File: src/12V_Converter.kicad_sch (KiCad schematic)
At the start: 37 parts, among them M4 CSD19534Q5A, M5 NVMFS6H836NLT1G, U2 LM5190RGYR_(20V-50V)

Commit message: Updated symbols
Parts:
- removed M5: NVMFS6H836NLT1G, PowerPCB_Footprints:NVMFS6H836NLT1G, symbol Schlib1:NVMFS6H836NLT1G
- removed Net Tie1: 0, powerDristributionBoard-import-fps:RESC0603X28X15NL05T05, symbol Altium Content Vault:RES
- added M3: NVMFS6H836NLT1G, PowerPCB_Footprints:NVMFS6H836NLT1G, symbol PowerPCB_Symbols:NVMFS6H836NLT1G
- added NT1: NetTie_2, symbol Device:NetTie_2
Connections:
- net GND: now also M3.1 (S), M3.2 (S), M3.3 (S), NT1.1
- net GNDA: now also NT1.2
- net at C18.2, L1.1, M4.1 (S)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: now also M3.5 (D)
- net at U2.9 (LO): now also M3.4 (G)

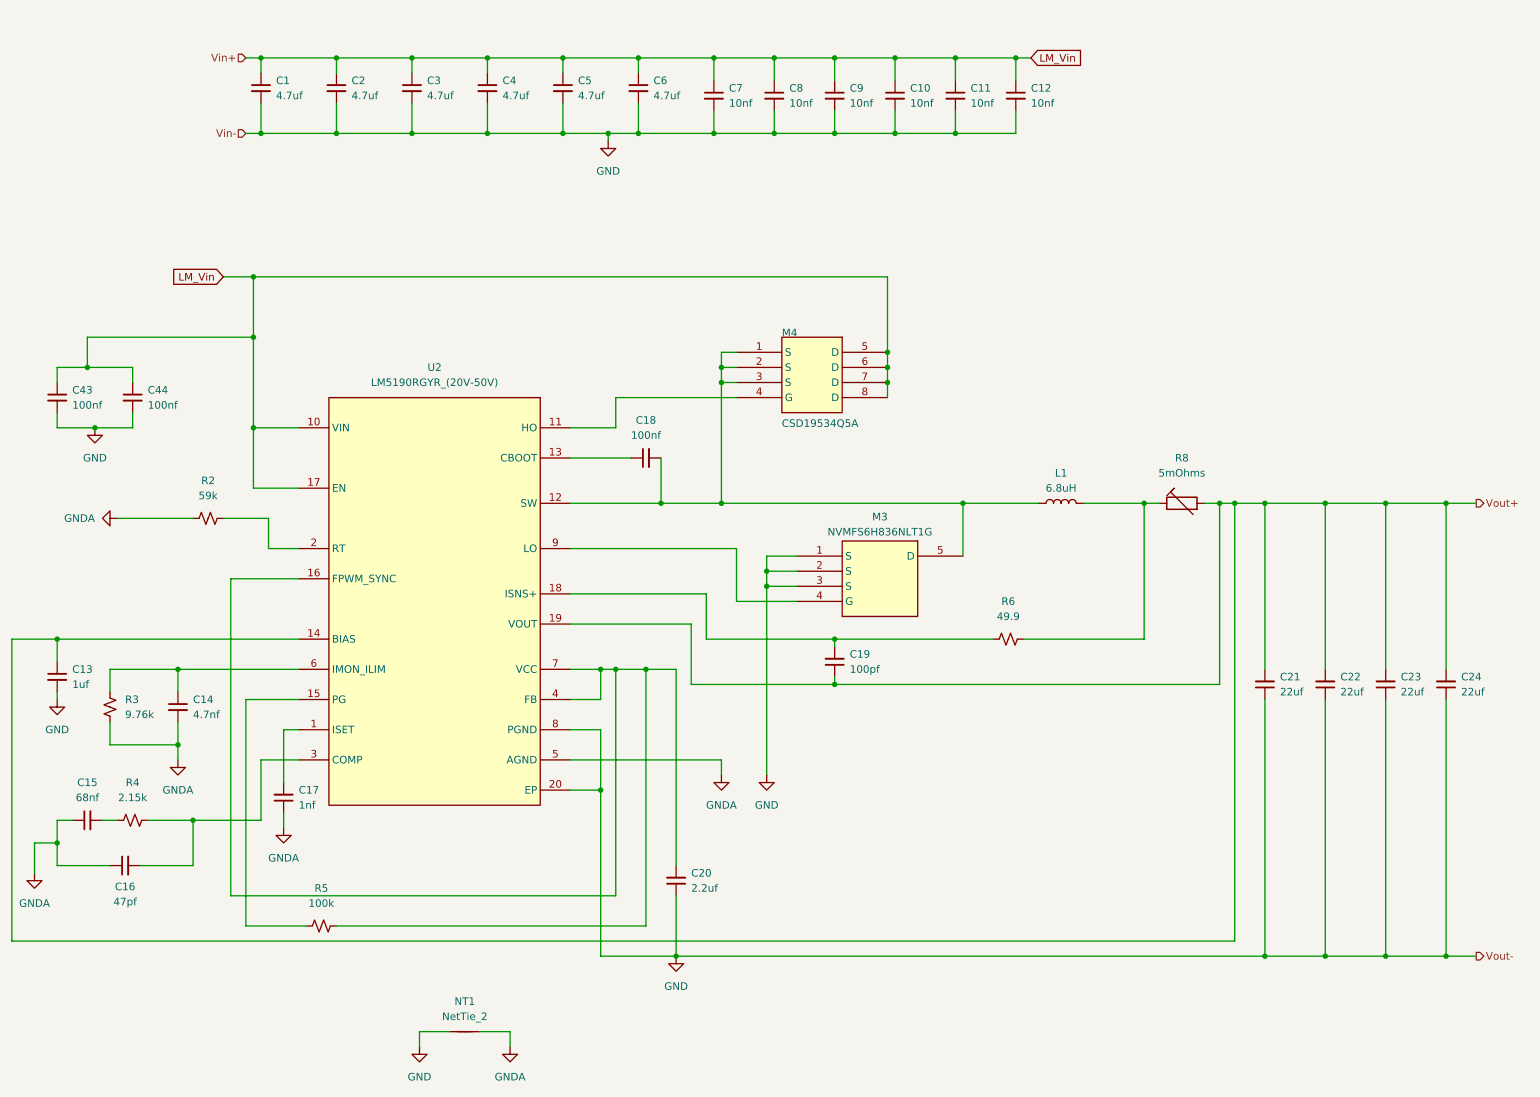
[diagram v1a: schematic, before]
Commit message: Added more components
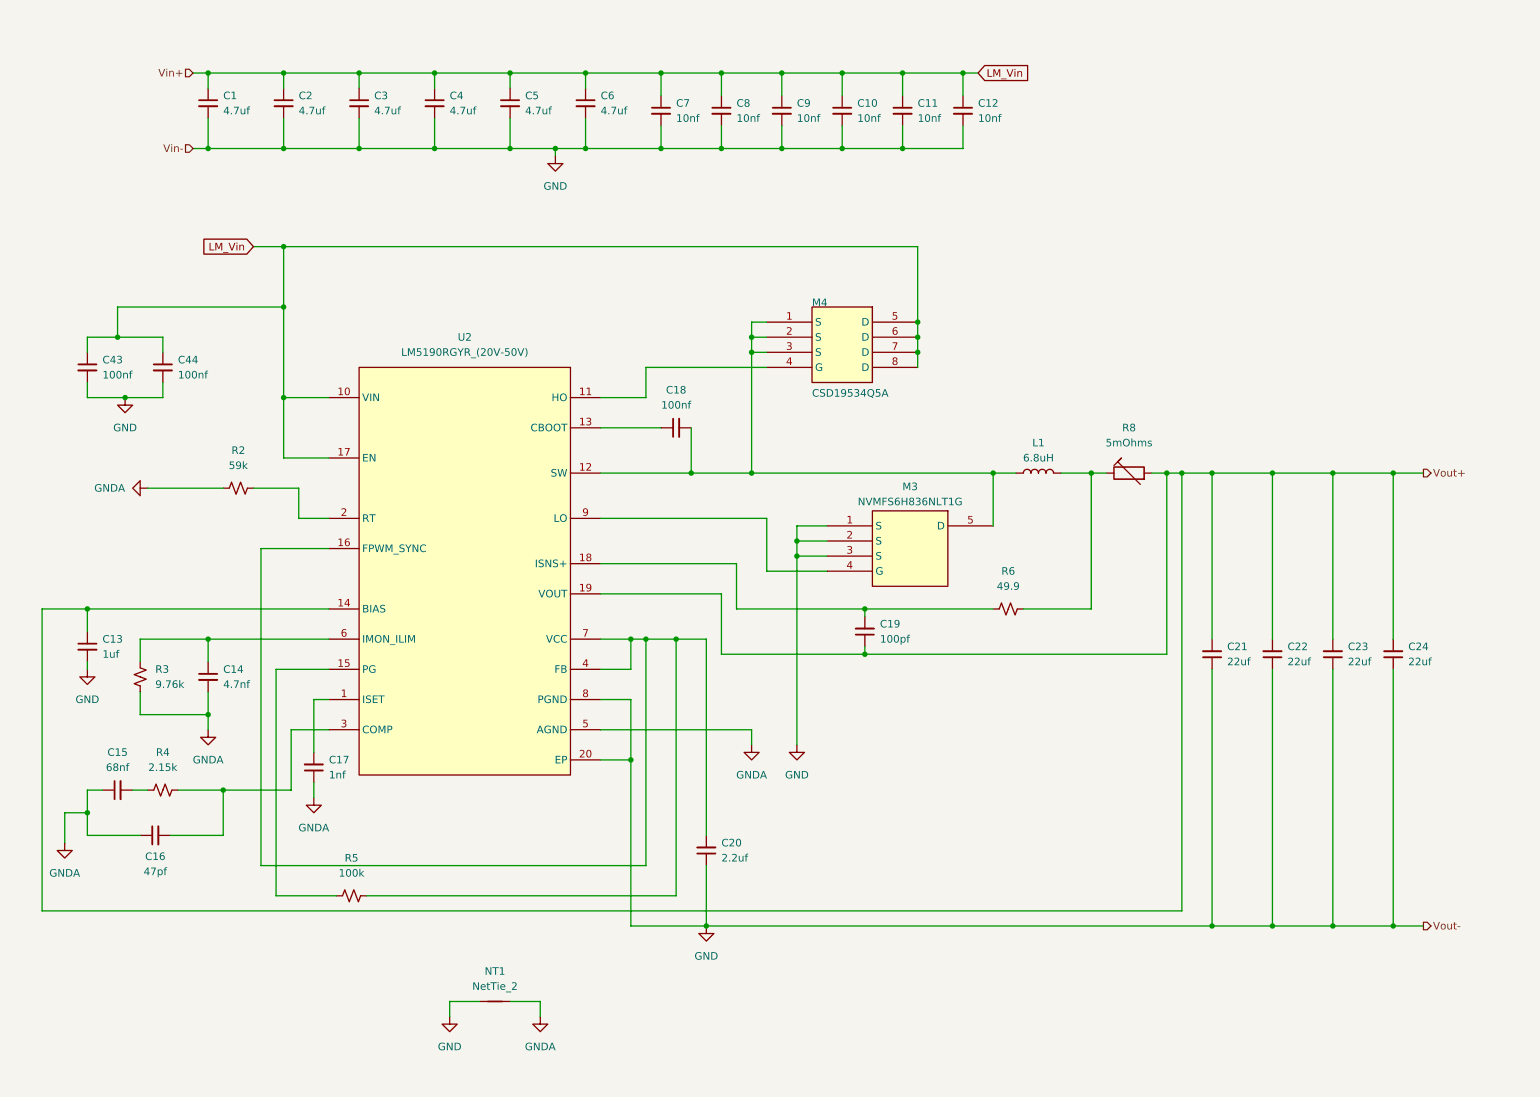
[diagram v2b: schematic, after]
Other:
- moved on the sheet: C1, C10, C11, C12, C13, C14, C15, C16, C17, C18, C19, C2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

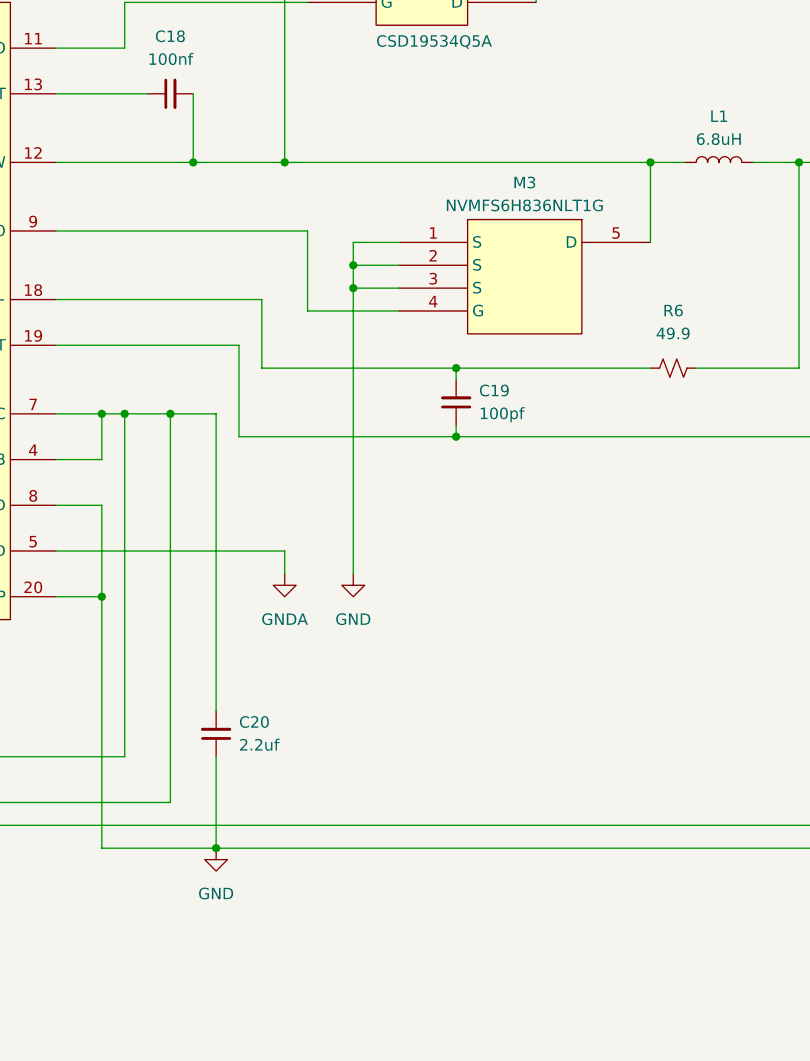
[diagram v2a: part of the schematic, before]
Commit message: Redesigned 5V regulator and edited libraries
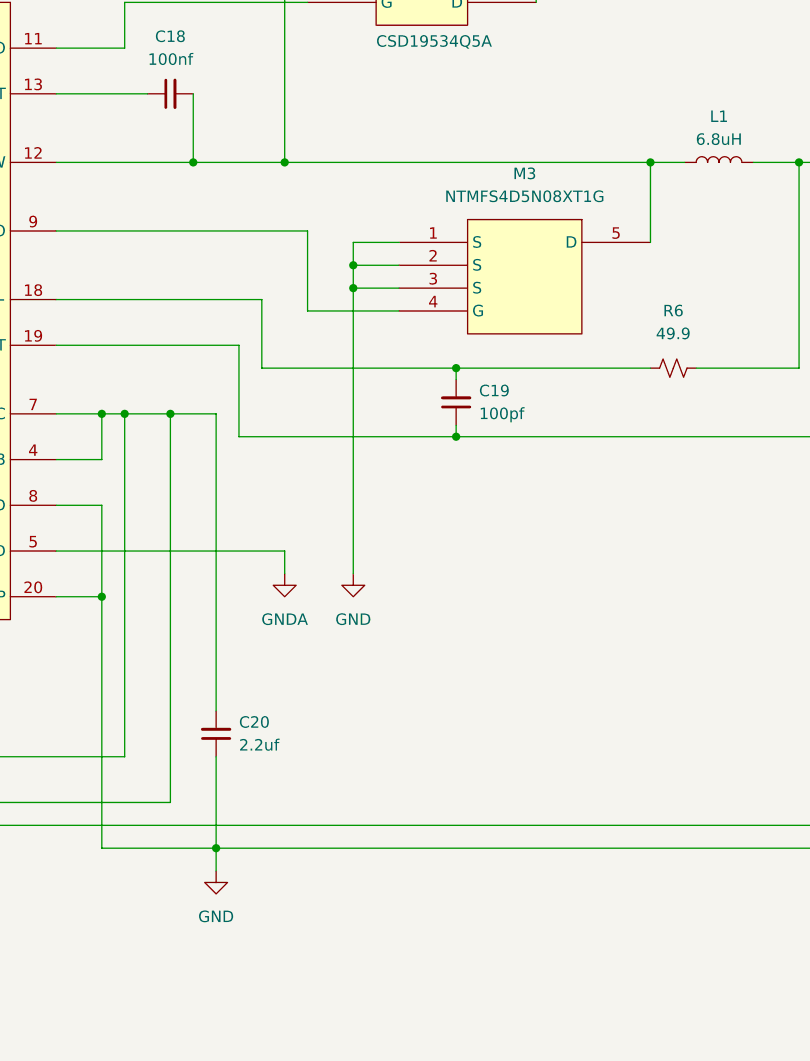
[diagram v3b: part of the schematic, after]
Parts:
- removed M3: NVMFS6H836NLT1G, PowerPCB_Footprints:NVMFS6H836NLT1G, symbol PowerPCB_Symbols:NVMFS6H836NLT1G
- added M3: NTMFS4D5N08XT1G, PowerPCB_Footprints:NTMFS4D5N08XT1G, symbol PowerPCB_Symbols:NTMFS4D5N08XT1G
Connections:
- net GND: now also M3.1 (S), M3.2 (S), M3.3 (S)
- net at C18.2, L1.1, M4.1 (S)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: now also M3.5 (D)
- net at U2.9 (LO): now also M3.4 (G)
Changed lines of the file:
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@@
 	(wire
 		(pts
+			(xy 132.08 170.18) (xy 132.08 167.64)
+		)
+		(stroke
+			(width 0)
+			(type default)
+		)
+	)
+	(wire
+		(pts
 			(xy 247.65 167.64) (xy 247.65 124.46)
 		)
@@
 	)
 	(symbol
+		(lib_id "PowerPCB_Symbols:NTMFS4D5N08XT1G")
+		(at 172.72 113.03 0)
+		(unit 1)
+		(body_style 1)
+		(exclude_from_sim no)
+		(in_bom yes)
+		(on_board yes)
+		(in_pos_files yes)
+		(dnp no)
+		(fields_autoplaced yes)
+		(property "Reference" "M3"
+			(at 166.37 92.71 0)
+			(show_name no)
+			(do_not_autoplace no)
+			(effects
+				(font
+					(size 1.27 1.27)
+				)
+			)
+		)
+		(property "Value" "NTMFS4D5N08XT1G"
+			(at 166.37 95.25 0)
+			(show_name no)
+			(do_not_autoplace no)
+			(effects
+				(font
+					(size 1.27 1.27)
+				)
+			)
+		)
+		(property "Footprint" "PowerPCB_Footprints:NTMFS4D5N08XT1G"
+			(at 172.72 113.03 0)
+			(hide yes)
+			(show_name no)
+			(do_not_autoplace no)
+			(effects
+				(font
+					(size 1.27 1.27)
+				)
+			)
+		)
+		(property "Datasheet" ""
+			(at 172.72 113.03 0)
+			(hide yes)
+			(show_name no)
+			(do_not_autoplace no)
+			(effects
+				(font
+					(size 1.27 1.27)
+				)
+			)
+		)
+		(property "Description" ""
+			(at 172.72 113.03 0)
+			(hide yes)
+			(show_name no)
+			(do_not_autoplace no)
+			(effects
+				(font
+					(size 1.27 1.27)
+				)
+			)
+		)
+		(pin "1"
+		)
+		(pin "4"
+		)
+		(pin "3"
+		)
+		(pin "2"
+		)
+		(pin "5"
+		)
+		(instances
+			(project "powerDristributionBoard"
+				(path "/501e9f3f-9bfa-47dd-b56d-5fd6974f0d03/8cad4ca2-ba0b-4eb3-ba1b-4233b97b1d3e"
+					(reference "M3")
+					(unit 1)
+				)
+			)
+		)
+	)
+	(symbol
 		(lib_id "Device:C_Small")
 		(at 48.26 29.21 0)
@@
 	)
 	(symbol
-		(lib_id "PowerPCB_Symbols:NVMFS6H836NLT1G")
-		(at 172.72 113.03 0)
-		(unit 1)
-		(body_style 1)
-		(exclude_from_sim no)
-		(in_bom yes)
-		(on_board yes)
-		(in_pos_files yes)
-		(dnp no)
-		(property "Reference" "M3"
-			(at 166.37 93.726 0)
-			(show_name no)
-			(do_not_autoplace no)
-			(effects
-				(font
-					(size 1.27 1.27)
-				)
-			)
-		)
-		(property "Value" "NVMFS6H836NLT1G"
-			(at 166.37 96.266 0)
-			(show_name no)
-			(do_not_autoplace no)
-			(effects
-				(font
-					(size 1.27 1.27)
-				)
-			)
-		)
-		(property "Footprint" "PowerPCB_Footprints:NVMFS6H836NLT1G"
-			(at 172.72 113.03 0)
-			(hide yes)
-			(show_name no)
-			(do_not_autoplace no)
-			(effects
-				(font
-					(size 1.27 1.27)
-				)
-			)
-		)
-		(property "Datasheet" ""
-			(at 172.72 113.03 0)
-			(hide yes)
-			(show_name no)
-			(do_not_autoplace no)
-			(effects
-				(font
-					(size 1.27 1.27)
-				)
-			)
-		)
-		(property "Description" ""
-			(at 172.72 113.03 0)
-			(hide yes)
-			(show_name no)
-			(do_not_autoplace no)
-			(effects
-				(font
-					(size 1.27 1.27)
-				)
-			)
-		)
-		(pin "1"
-		)
-		(pin "5"
-		)
-		(pin "3"
-		)
-		(pin "4"
-		)
-		(pin "2"
-		)
-		(instances
-			(project "powerDristributionBoard"
-				(path "/501e9f3f-9bfa-47dd-b56d-5fd6974f0d03/8cad4ca2-ba0b-4eb3-ba1b-4233b97b1d3e"
-					(reference "M3")
-					(unit 1)
-				)
-			)
-		)
-	)
-	(symbol
 		(lib_id "Device:C_Small")
 		(at 99.06 29.21 0)
@@
 	(symbol
 		(lib_id "power:GND")
-		(at 132.08 167.64 0)
+		(at 132.08 170.18 0)
 		(unit 1)
 		(body_style 1)
@@
 		(fields_autoplaced yes)
 		(property "Reference" "#PWR06"
-			(at 132.08 173.99 0)
+			(at 132.08 176.53 0)
 			(hide yes)
 			(show_name no)
@@
 		)
 		(property "Value" "GND"
-			(at 132.08 172.72 0)
+			(at 132.08 175.26 0)
 			(show_name no)
 			(do_not_autoplace no)
@@
 		)
 		(property "Footprint" ""
-			(at 132.08 167.64 0)
+			(at 132.08 170.18 0)
 			(hide yes)
 			(show_name no)
@@
 		)
 		(property "Datasheet" ""
-			(at 132.08 167.64 0)
+			(at 132.08 170.18 0)
 			(hide yes)
 			(show_name no)
@@
 		)
 		(property "Description" "Power symbol creates a global label with name \"GND\" , ground"
-			(at 132.08 167.64 0)
+			(at 132.08 170.18 0)
 			(hide yes)
 			(show_name no)

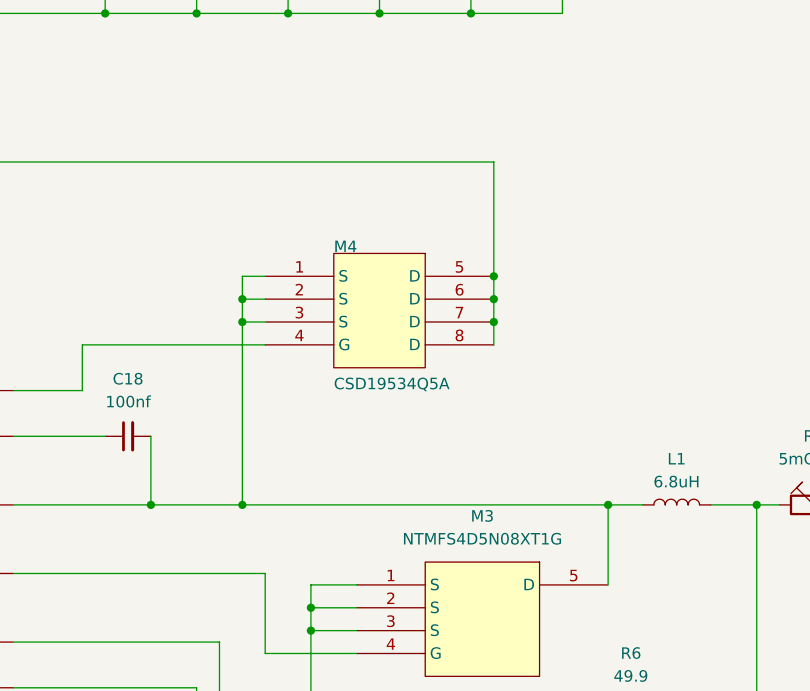
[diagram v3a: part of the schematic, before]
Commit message: Redesigned 5V regulator and added more parts
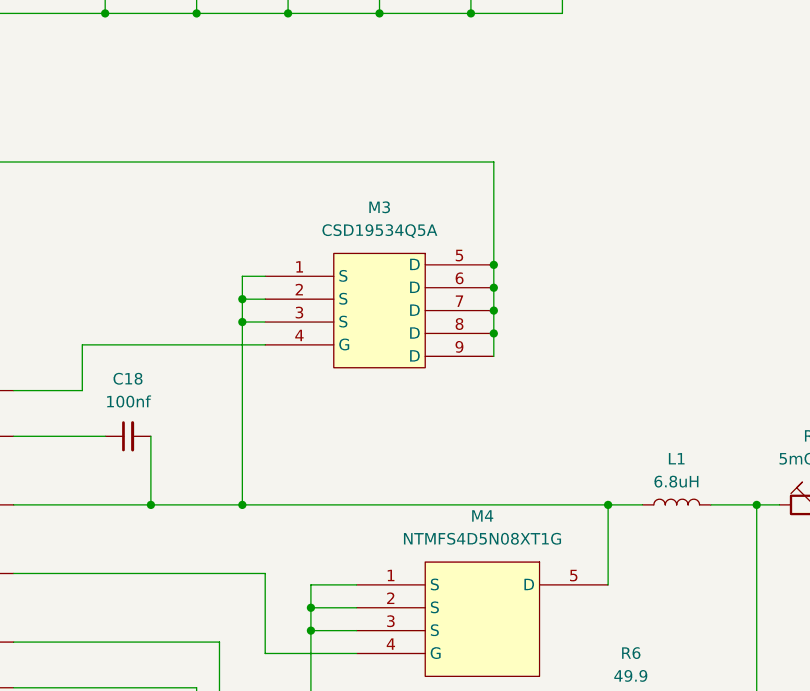
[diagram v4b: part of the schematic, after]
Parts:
- removed M4: CSD19534Q5A, PowerPCB_Footprints:CSD19534Q5A, symbol Schlib1:CSD19534Q5A
- added M3: CSD19534Q5A, PowerPCB_Footprints:CSD19534Q5A, symbol PowerPCB_Symbols:CSD19534Q5A
- renumbered M3 to M4
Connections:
- net LM_Vin: now also M3.5 (D), M3.6 (D), M3.7 (D), M3.8 (D), M3.9 (D)
- net at C18.2, L1.1, M4.5 (D)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: now also M3.1 (S), M3.2 (S), M3.3 (S)
- net at U2.11 (HO): now also M3.4 (G)

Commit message: Finalized schematic
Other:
- moved on the sheet: R3

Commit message: Edited PCB layout
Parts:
- C32: renamed from C21; now not fitted
- C33: renamed from C22; now not fitted
- C34: renamed from C23; now not fitted
- C35: renamed from C24; now not fitted
- renumbered C43 to C10, C13 to C11, C15 to C12, C44 to C13, C16 to C14, C1 to C15, C14 to C16, C2 to C17, C17 to C18, C3 to C19, C4 to C20, C5 to C21, C6 to C22, C7 to C23, C18 to C24, C20 to C25, C8 to C26, C9 to C27, C10 to C28, C19 to C29, C11 to C30, C12 to C31, R3 to R10, R4 to R11, R2 to R12, R5 to R13, R6 to R14, R8 to R15

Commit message: Edited PCB layout
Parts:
- C32, C33, C34, C35: now fitted
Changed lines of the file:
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@@
 		(on_board yes)
 		(in_pos_files yes)
-		(dnp yes)
+		(dnp no)
 		(fields_autoplaced yes)
 		(property "Reference" "C34"
@@
 		(on_board yes)
 		(in_pos_files yes)
-		(dnp yes)
+		(dnp no)
 		(fields_autoplaced yes)
 		(property "Reference" "C35"
@@
 		(on_board yes)
 		(in_pos_files yes)
-		(dnp yes)
+		(dnp no)
 		(fields_autoplaced yes)
 		(property "Reference" "C32"
@@
 		(on_board yes)
 		(in_pos_files yes)
-		(dnp yes)
+		(dnp no)
 		(fields_autoplaced yes)
 		(property "Reference" "C33"

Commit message: GG
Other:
- moved on the sheet: C10, C11, C12, C13, C14, C15, C16, C17, C18, C19, C20, C21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
